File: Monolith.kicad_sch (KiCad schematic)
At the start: 20 parts, among them J2 Conn_01x11, J3 Conn_01x11, J4 Conn_01x02, J5 Conn_01x02, J6 Conn_01x07, U1 ADS1299IPAGR, U12 ESP32-S3-MINI-1

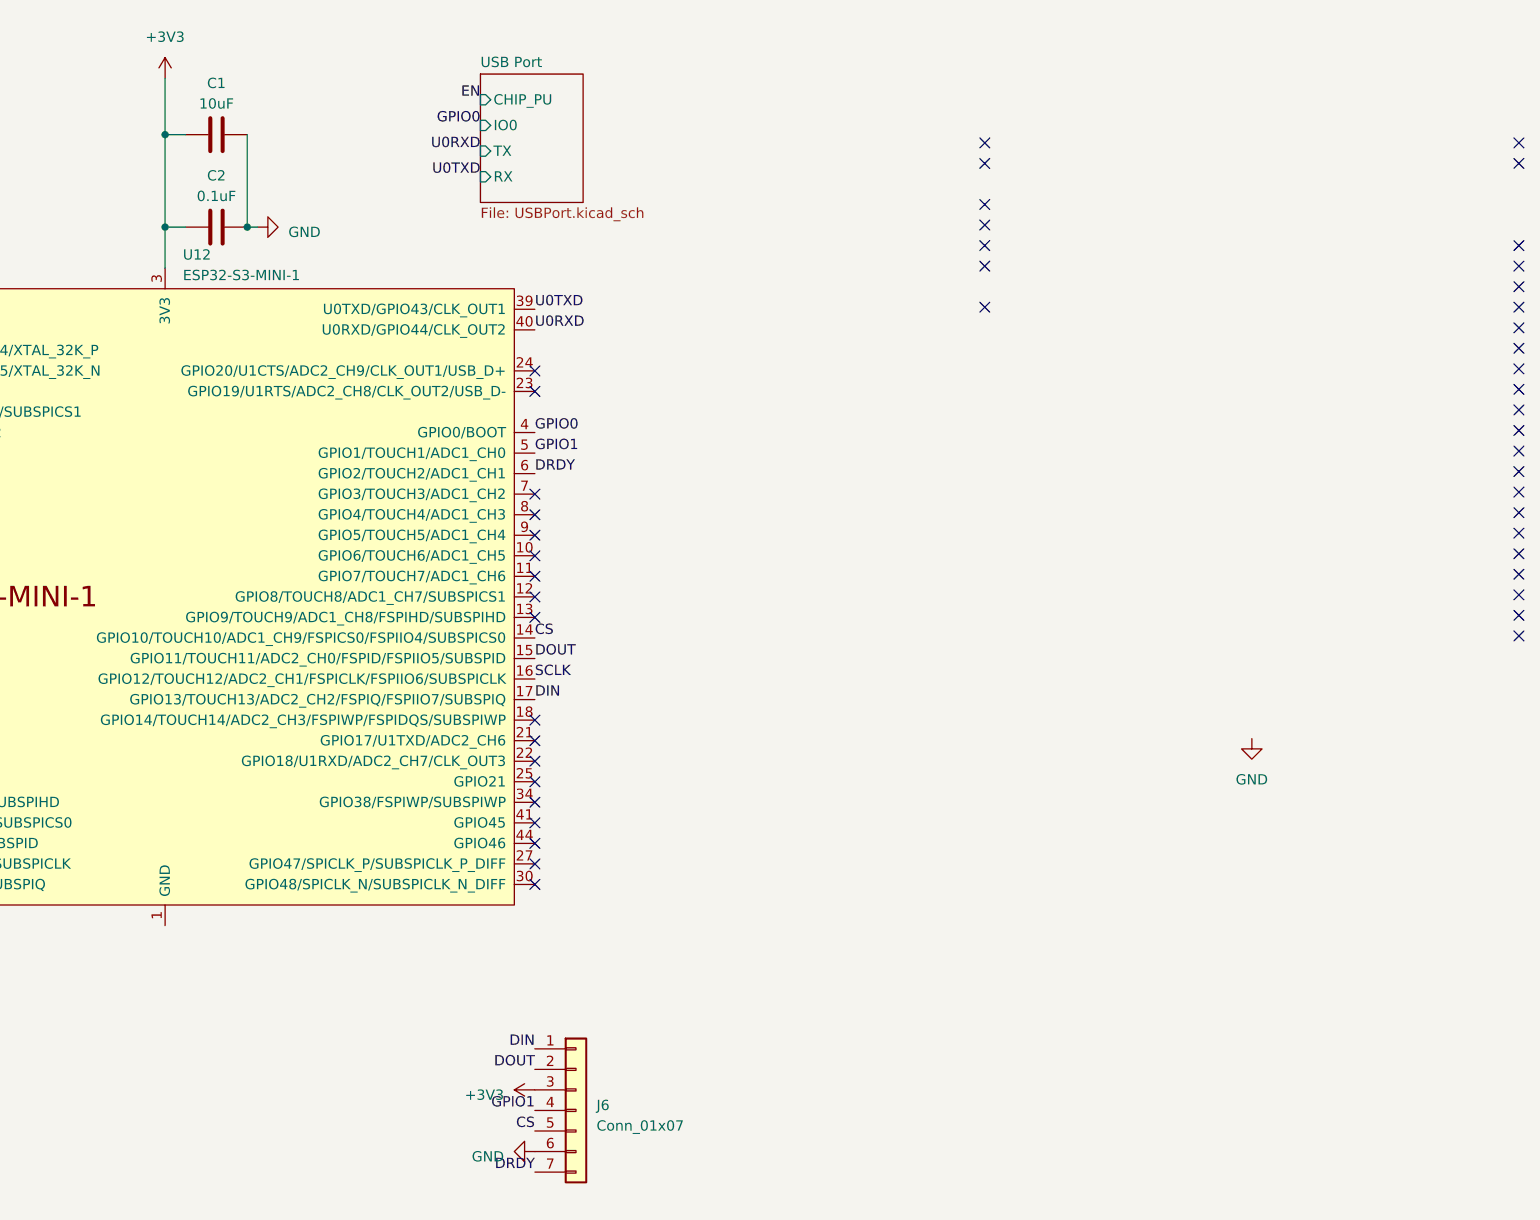
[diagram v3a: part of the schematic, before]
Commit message: add pin for SCLK on header
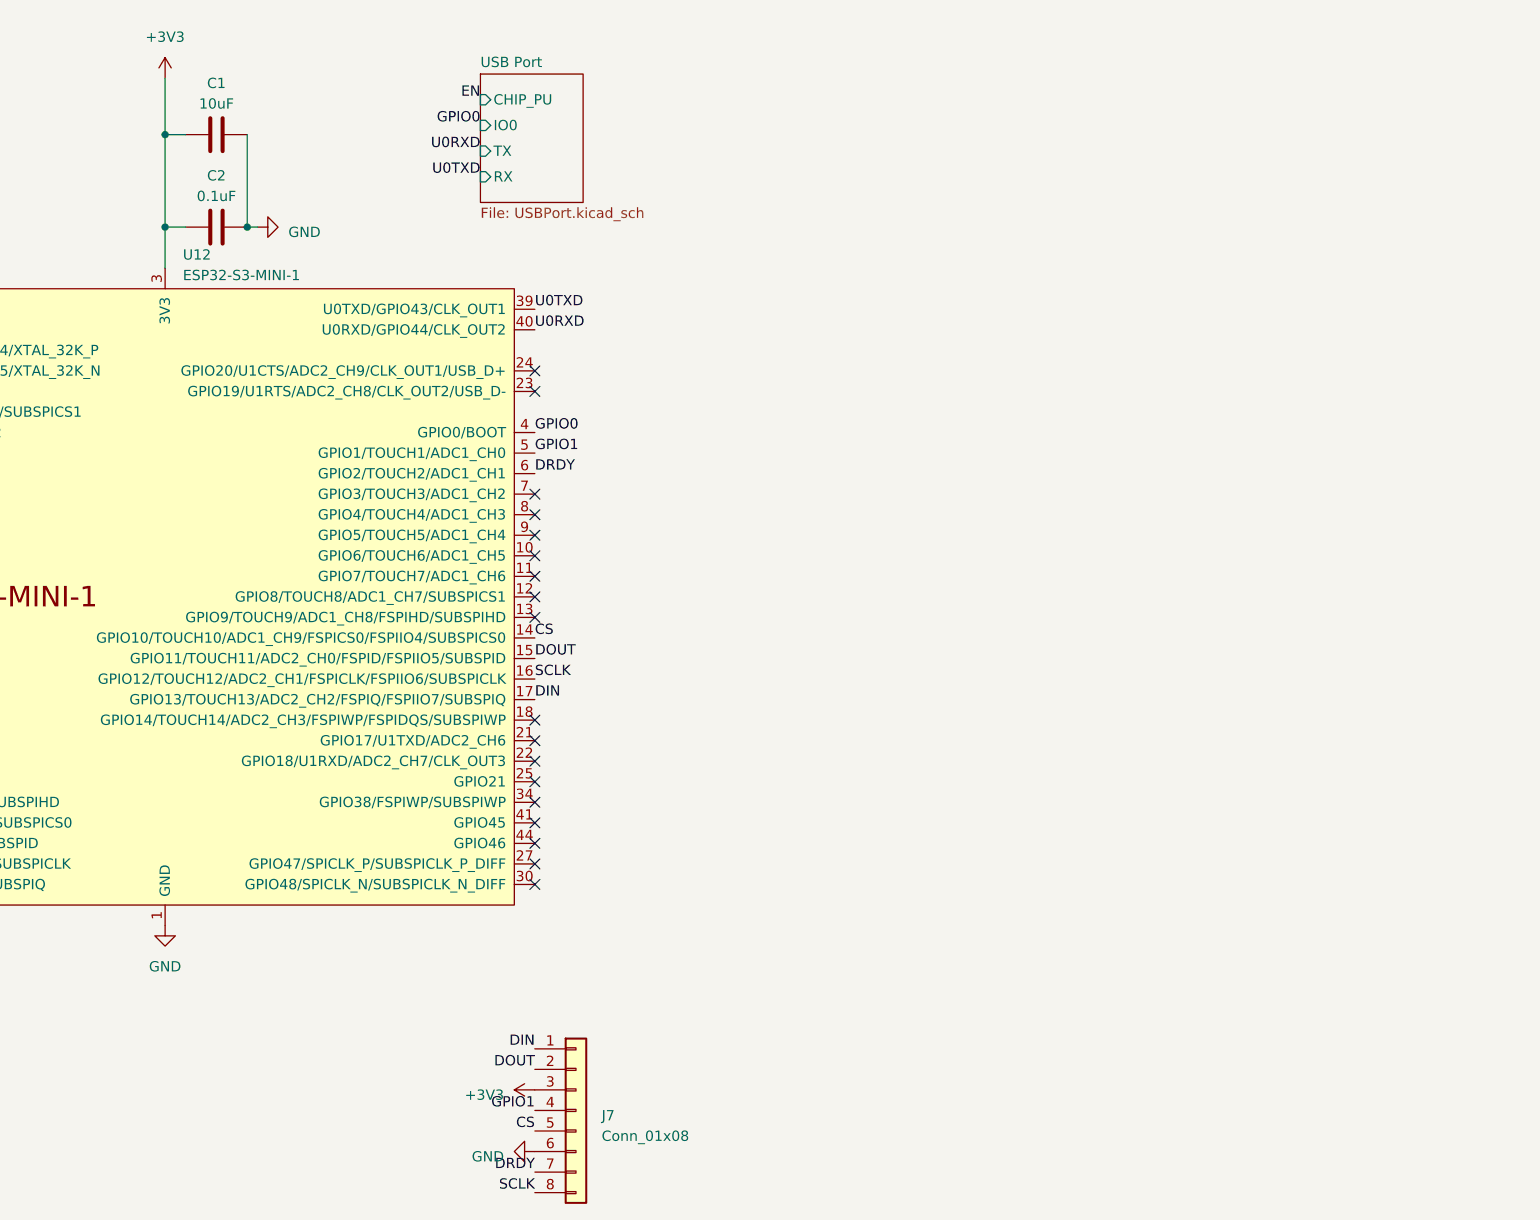
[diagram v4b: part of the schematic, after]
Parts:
- removed J6: Conn_01x07, Connector_PinSocket_2.54mm:PinSocket_1x07_P2.54mm_Vertical, symbol Connector_Generic:Conn_01x07
- added J7: Conn_01x08, symbol Connector_Generic:Conn_01x08
- U12: LCSC (none) -> C2913206
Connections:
- net +3V3: now also J7.3 (Pin_3)
- net CS: now also J7.5 (Pin_5)
- net DIN: now also J7.1 (Pin_1)
- net DOUT: now also J7.2 (Pin_2)
- net DRDY: now also J7.7 (Pin_7)
- net GND: now also U12.1 (GND), U12.2 (GND), U12.42 (GND), U12.43 (GND), U12.46 (GND), U12.47 (GND), U12.48 (GND), U12.49 (GND), U12.50 (GND), U12.51 (GND), U12.52 (GND), U12.53 (GND), U12.54 (GND), U12.55 (GND), U12.56 (GND), U12.57 (GND), U12.58 (GND), U12.59 (GND), U12.60 (GND), U12.61 (GND), U12.62 (GND), U12.63 (GND), U12.64 (GND), U12.65 (GND), J7.6 (Pin_6)
- net GPIO1: now also J7.4 (Pin_4)
- net SCLK: now also J7.8 (Pin_8)
- no-connect marks 67 -> 38
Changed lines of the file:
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@@
   (no_connect (at 102.87 120.65))
   (no_connect (at 259.715 83.82))
-  (no_connect (at 315.341 45.466))
-  (no_connect (at 381.381 75.946))
-  (no_connect (at 381.381 48.006))
   (no_connect (at 168.275 71.12))
   (no_connect (at 168.275 124.46))
-  (no_connect (at 381.381 91.186))
-  (no_connect (at 315.341 53.086))
   (no_connect (at 259.715 76.2))
   (no_connect (at 168.275 68.58))
-  (no_connect (at 315.341 35.306))
   (no_connect (at 168.275 114.3))
   (no_connect (at 259.715 91.44))
-  (no_connect (at 381.381 35.306))
   (no_connect (at 259.715 124.46))
   (no_connect (at 168.275 66.04))
-  (no_connect (at 381.381 58.166))
   (no_connect (at 259.715 116.84))
-  (no_connect (at 381.381 65.786))
   (no_connect (at 259.715 111.76))
   (no_connect (at 168.275 119.38))
   (no_connect (at 102.87 123.19))
-  (no_connect (at 315.341 40.386))
   (no_connect (at 259.715 104.14))
   (no_connect (at 259.715 60.96))
-  (no_connect (at 381.381 50.546))
   (no_connect (at 259.715 78.74))
   (no_connect (at 138.43 123.19))
-  (no_connect (at 381.381 73.406))
-  (no_connect (at 381.381 83.566))
   (no_connect (at 102.87 110.49))
-  (no_connect (at 381.381 81.026))
-  (no_connect (at 381.381 45.466))
   (no_connect (at 102.87 49.53))
-  (no_connect (at 381.381 93.726))
   (no_connect (at 168.275 111.76))
   (no_connect (at 259.715 86.36))
@@
   (no_connect (at 259.715 81.28))
   (no_connect (at 259.715 88.9))
-  (no_connect (at 381.381 32.766))
-  (no_connect (at 315.341 32.766))
   (no_connect (at 102.87 54.61))
   (no_connect (at 259.715 114.3))
   (no_connect (at 168.275 58.42))
   (no_connect (at 259.715 119.38))
-  (no_connect (at 381.381 68.326))
   (no_connect (at 168.275 60.96))
   (no_connect (at 138.43 120.65))
   (no_connect (at 168.275 121.92))
-  (no_connect (at 381.381 60.706))
-  (no_connect (at 381.381 53.086))
-  (no_connect (at 315.341 42.926))
   (no_connect (at 138.43 46.99))
-  (no_connect (at 381.381 63.246))
-  (no_connect (at 381.381 88.646))
   (no_connect (at 259.715 121.92))
   (no_connect (at 259.715 106.68))
-  (no_connect (at 381.381 86.106))
-  (no_connect (at 381.381 78.486))
   (no_connect (at 168.275 116.84))
-  (no_connect (at 381.381 70.866))
-  (no_connect (at 381.381 55.626))
-  (no_connect (at 315.341 48.006))
   (no_connect (at 168.275 73.66))
   (wire (pts (xy 95.25 138.43) (xy 102.87 138.43))
@@
   )
   (label "5P" (at 26.67 98.425 180) (fields_autoplaced)
+    (effects (font (size 1.27 1.27)) (justify right bottom))
+  )
+  (label "SCLK" (at 259.715 162.56 180) (fields_autoplaced)
     (effects (font (size 1.27 1.27)) (justify right bottom))
   )
@@
     )
   )
+  (symbol (lib_id "Connector_Generic:Conn_01x08") (at 264.795 152.4 0) (unit 1)
+    (in_bom yes) (on_board yes) (dnp no) (fields_autoplaced)
+    (property "Reference" "J7" (at 267.97 153.035 0)
+      (effects (font (size 1.27 1.27)) (justify left))
+    )
+    (property "Value" "Conn_01x08" (at 267.97 155.575 0)
+      (effects (font (size 1.27 1.27)) (justify left))
+    )
+    (property "Footprint" "" (at 264.795 152.4 0)
+      (effects (font (size 1.27 1.27)) hide)
+    )
+    (property "Datasheet" "~" (at 264.795 152.4 0)
+      (effects (font (size 1.27 1.27)) hide)
+    )
+    (pin "1")
+    (pin "2")
+    (pin "3")
+    (pin "4")
+    (pin "5")
+    (pin "6")
+    (pin "7")
+    (pin "8")
+    (instances
+      (project "Monolith"
+        (path "/a4ecfbe3-0f16-403e-8cdc-2760bb3b2c3f"
+          (reference "J7") (unit 1)
+        )
+      )
+    )
+  )
   (symbol (lib_id "power:+3V3") (at 102.87 41.91 90) (unit 1)
     (in_bom yes) (on_board yes) (dnp no)
@@
     )
   )
-  (symbol (lib_id "power:GND") (at 348.361 106.426 0) (unit 1)
+  (symbol (lib_id "power:GND") (at 213.995 129.54 0) (unit 1)
     (in_bom yes) (on_board yes) (dnp no)
-    (property "Reference" "#PWR011" (at 348.361 112.776 0)
-      (effects (font (size 1.27 1.27)) hide)
-    )
-    (property "Value" "GND" (at 348.361 111.506 0)
-      (effects (font (size 1.27 1.27)))
-    )
-    (property "Footprint" "" (at 348.361 106.426 0)
-      (effects (font (size 1.27 1.27)) hide)
-    )
-    (property "Datasheet" "" (at 348.361 106.426 0)
+    (property "Reference" "#PWR011" (at 213.995 135.89 0)
+      (effects (font (size 1.27 1.27)) hide)
+    )
+    (property "Value" "GND" (at 213.995 134.62 0)
+      (effects (font (size 1.27 1.27)))
+    )
+    (property "Footprint" "" (at 213.995 129.54 0)
+      (effects (font (size 1.27 1.27)) hide)
+    )
+    (property "Datasheet" "" (at 213.995 129.54 0)
       (effects (font (size 1.27 1.27)) hide)
     )
@@
     )
     (property "Datasheet" "https://www.espressif.com/sites/default/files/documentation/esp32-s3-mini-1_mini-1u_datasheet_en.pdf" (at 213.995 147.32 0)
+      (effects (font (size 1.27 1.27)) hide)
+    )
+    (property "LCSC" "C2913206" (at 213.995 88.9 0)
       (effects (font (size 1.27 1.27)) hide)
     )
@@
         )
       )
-    )
-  )
-  (symbol (lib_id "Connector_Generic:Conn_01x07") (at 264.795 152.4 0) (unit 1)
-    (in_bom yes) (on_board yes) (dnp no) (fields_autoplaced)
-    (property "Reference" "J6" (at 267.335 151.765 0)
-      (effects (font (size 1.27 1.27)) (justify left))
-    )
-    (property "Value" "Conn_01x07" (at 267.335 154.305 0)
-      (effects (font (size 1.27 1.27)) (justify left))
-    )
-    (property "Footprint" "Connector_PinSocket_2.54mm:PinSocket_1x07_P2.54mm_Vertical" (at 264.795 152.4 0)
-      (effects (font (size 1.27 1.27)) hide)
-    )
-    (property "Datasheet" "~" (at 264.795 152.4 0)
-      (effects (font (size 1.27 1.27)) hide)
-    )
-    (pin "1")
-    (pin "2")
-    (pin "3")
-    (pin "4")
-    (pin "5")
-    (pin "6")
-    (pin "7")
-    (instances
-      (project "Monolith"
-        (path "/a4ecfbe3-0f16-403e-8cdc-2760bb3b2c3f"
-          (reference "J6") (unit 1)
-        )
-      )

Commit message: stuff
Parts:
- J7: footprint (none) -> Connector_PinHeader_2.54mm:PinHeader_1x08_P2.54mm_Vertical
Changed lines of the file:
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@@
       (effects (font (size 1.27 1.27)) (justify left))
     )
-    (property "Footprint" "" (at 264.795 152.4 0)
+    (property "Footprint" "Connector_PinHeader_2.54mm:PinHeader_1x08_P2.54mm_Vertical" (at 264.795 152.4 0)
       (effects (font (size 1.27 1.27)) hide)
     )
